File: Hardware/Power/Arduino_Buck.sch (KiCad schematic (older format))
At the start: 10 parts, among them Q3 2N7000, Q4 PJM2301PSA-S

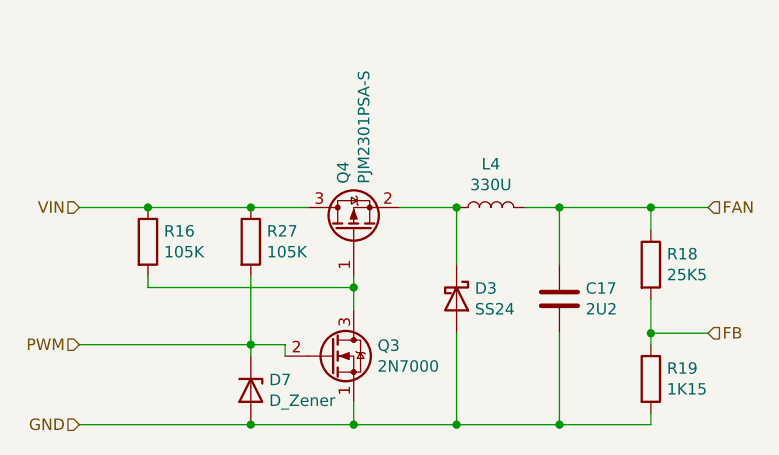
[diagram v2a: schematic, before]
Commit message: Fixed Power Board Errata
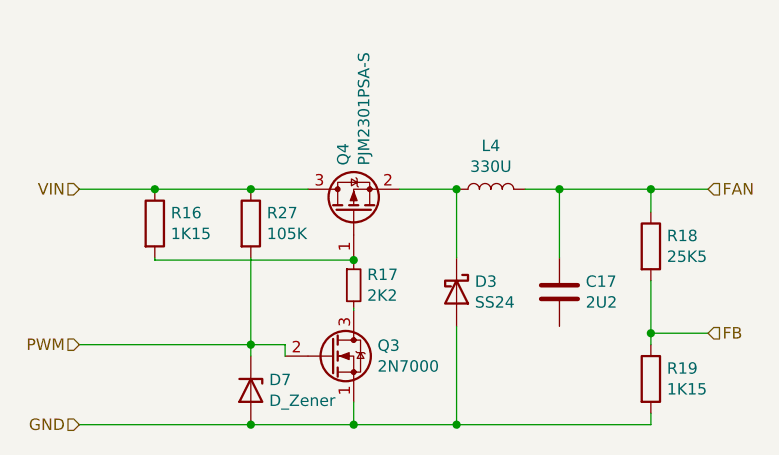
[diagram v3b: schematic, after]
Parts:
- added R17: 2K2, Resistor_SMD:R_0603_1608Metric_Pad1.05x0.95mm_HandSolder, symbol Device:R_Small
- R16: value 105K -> 1K15; Manufacturer_Part_Number RC0603FR-07105KL -> (none)
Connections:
- net GND: no longer C17.2
- net at Q4.1 (G), R16.2: now also R17.1; no longer Q3.3 (D)
- new net: Q3.3 (D), R17.2
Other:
- moved on the sheet: C17, D3, L4, Q4, R18, R27
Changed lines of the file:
@@
 $Descr A4 11693 8268
 encoding utf-8
-Sheet 5 7
+Sheet 4 7
 Title ""
 Date ""
@@
 Comment4 ""
 $EndDescr
-Text HLabel 4450 3450 0    50   Input ~ 0
-VIN
-Text HLabel 7200 3450 2    50   Input ~ 0
-FAN
 Text HLabel 4450 4400 0    50   Input ~ 0
 GND
 Text HLabel 7200 4000 2    50   Input ~ 0
 FB
-$Comp
-L Device:L L4
-U 1 1 5F8E9295
-P 6250 3450
-F 0 "L4" V 6440 3450 50  0000 C CNN
-F 1 "330U" V 6349 3450 50  0000 C CNN
-F 2 "ArduinoLamp:SLD10" H 6250 3450 50  0001 C CNN
-F 3 "~" H 6250 3450 50  0001 C CNN
-F 4 "SLD10D40S331MTT" H 6250 3450 50  0001 C CNN "Manufacturer_Part_Number"
-	1    6250 3450
-	0    -1   -1   0
-$EndComp
-$Comp
-L Device:D_Schottky D3
-U 1 1 5F8E9922
-P 6100 3850
-F 0 "D3" V 6054 3930 50  0000 L CNN
-F 1 "SS24" V 6145 3930 50  0000 L CNN
-F 2 "ArduinoLamp:D_SMA_Handsoldering_Shortened" H 6100 3850 50  0001 C CNN
-F 3 "~" H 6100 3850 50  0001 C CNN
-F 4 "" H 6100 3850 50  0001 C CNN "Mouser Part Number"
-F 5 "C181203" H 6100 3850 50  0001 C CNN "Arrow Part Number"
-	1    6100 3850
-	0    1    1    0
-$EndComp
-$Comp
-L Device:C C17
-U 1 1 5F8EC349
-P 6550 3850
-F 0 "C17" H 6665 3896 50  0000 L CNN
-F 1 "2U2" H 6665 3805 50  0000 L CNN
-F 2 "Capacitor_SMD:C_0805_2012Metric_Pad1.15x1.40mm_HandSolder" H 6588 3700 50  0001 C CNN
-F 3 "~" H 6550 3850 50  0001 C CNN
-F 4 "C0805X5R225K500NT" H 6550 3850 50  0001 C CNN "Manufacturer_Part_Number"
-	1    6550 3850
-	1    0    0    -1
-$EndComp
-$Comp
-L Device:R R18
-U 1 1 5F8ECD7F
-P 6950 3700
-F 0 "R18" H 7020 3746 50  0000 L CNN
-F 1 "25K5" H 7020 3655 50  0000 L CNN
-F 2 "Resistor_SMD:R_0603_1608Metric_Pad1.05x0.95mm_HandSolder" V 6880 3700 50  0001 C CNN
-F 3 "~" H 6950 3700 50  0001 C CNN
-F 4 "RS-05K2552FT" H 6950 3700 50  0001 C CNN "Manufacturer_Part_Number"
-	1    6950 3700
-	1    0    0    -1
-$EndComp
 $Comp
 L Device:R R19
@@
 Wire Wire Line
 	6950 4350 6950 4400
-Wire Wire Line
-	6950 4400 6550 4400
-Connection ~ 6550 4400
-Wire Wire Line
-	6550 3700 6550 3450
-Wire Wire Line
-	6550 3450 6950 3450
-Wire Wire Line
-	6950 3450 6950 3550
-Connection ~ 6950 3450
-Wire Wire Line
-	6950 3450 7200 3450
-Wire Wire Line
-	6400 3450 6550 3450
-Connection ~ 6550 3450
-Wire Wire Line
-	6100 3450 6100 3700
-$Comp
-L Device:R R27
-U 1 1 5FAF10C0
-P 5200 3600
-F 0 "R27" H 5270 3646 50  0000 L CNN
-F 1 "105K" H 5270 3555 50  0000 L CNN
-F 2 "Resistor_SMD:R_0603_1608Metric_Pad1.05x0.95mm_HandSolder" V 5130 3600 50  0001 C CNN
-F 3 "~" H 5200 3600 50  0001 C CNN
-F 4 "RC0603FR-07105KL" H 5200 3600 50  0001 C CNN "Manufacturer_Part_Number"
-	1    5200 3600
-	1    0    0    -1
-$EndComp
-$Comp
-L Device:R R16
-U 1 1 5F8FA0B3
-P 4750 3600
-F 0 "R16" H 4820 3646 50  0000 L CNN
-F 1 "105K" H 4820 3555 50  0000 L CNN
-F 2 "Resistor_SMD:R_0603_1608Metric_Pad1.05x0.95mm_HandSolder" V 4680 3600 50  0001 C CNN
-F 3 "~" H 4750 3600 50  0001 C CNN
-F 4 "RC0603FR-07105KL" H 4750 3600 50  0001 C CNN "Manufacturer_Part_Number"
-	1    4750 3600
-	1    0    0    -1
-$EndComp
 Connection ~ 5650 4400
-Connection ~ 6100 3450
-Wire Wire Line
-	5850 3450 6100 3450
 Connection ~ 6100 4400
-Wire Wire Line
-	6100 4400 6550 4400
 Wire Wire Line
 	5650 4400 6100 4400
@@
 	1    0    0    -1
 $EndComp
-Connection ~ 5200 3450
-Wire Wire Line
-	4450 3450 4750 3450
-Connection ~ 4750 3450
-Wire Wire Line
-	4750 3450 5200 3450
-Wire Wire Line
-	4750 3750 4750 3800
-Wire Wire Line
-	5200 3450 5450 3450
 Wire Wire Line
 	4450 4050 5200 4050
@@
 Wire Wire Line
 	5350 4050 5350 4100
-$Comp
-L Transistor_FET:TSM2301ACX Q4
-U 1 1 5F8E71B4
-P 5650 3550
-F 0 "Q4" H 5854 3596 50  0000 L CNN
-F 1 "PJM2301PSA-S" H 5854 3505 50  0000 L CNN
-F 2 "Package_TO_SOT_SMD:SOT-23" H 5850 3475 50  0001 L CIN
-F 3 "https://www.taiwansemi.com/products/datasheet/TSM2301A_C15.pdf" H 5650 3550 50  0001 L CNN
-F 4 "PJM2301PSA-S" H 5650 3550 50  0001 C CNN "Manufacturer_Part_Number"
-	1    5650 3550
-	0    -1   -1   0
-$EndComp
-Wire Wire Line
-	5200 3750 5200 4050
-Wire Wire Line
-	6100 4000 6100 4400
-Wire Wire Line
-	6550 4000 6550 4400
-Wire Wire Line
-	5650 3800 5650 3750
-Wire Wire Line
-	4750 3800 5650 3800
-Wire Wire Line
-	5650 3900 5650 3800
-Connection ~ 5650 3800
-Wire Wire Line
-	6950 3850 6950 4000
-Connection ~ 6950 4000
 Wire Wire Line
 	4450 4400 5200 4400
@@
 Wire Wire Line
 	5200 4400 5650 4400
+Wire Wire Line
+	4450 3370 4780 3370
+$Comp
+L Transistor_FET:TSM2301ACX Q4
+U 1 1 5F8E71B4
+P 5650 3470
+F 0 "Q4" H 5854 3516 50  0000 L CNN
+F 1 "PJM2301PSA-S" H 5854 3425 50  0000 L CNN
+F 2 "Package_TO_SOT_SMD:SOT-23" H 5850 3395 50  0001 L CIN
+F 3 "https://www.taiwansemi.com/products/datasheet/TSM2301A_C15.pdf" H 5650 3470 50  0001 L CNN
+F 4 "PJM2301PSA-S" H 5650 3470 50  0001 C CNN "Manufacturer_Part_Number"
+	1    5650 3470
+	0    -1   -1   0
+$EndComp
+Wire Wire Line
+	5200 3370 5450 3370
+Connection ~ 5200 3370
+Wire Wire Line
+	5850 3370 6100 3370
+$Comp
+L Device:R R27
+U 1 1 5FAF10C0
+P 5200 3520
+F 0 "R27" H 5270 3566 50  0000 L CNN
+F 1 "105K" H 5270 3475 50  0000 L CNN
+F 2 "Resistor_SMD:R_0603_1608Metric_Pad1.05x0.95mm_HandSolder" V 5130 3520 50  0001 C CNN
+F 3 "~" H 5200 3520 50  0001 C CNN
+F 4 "RC0603FR-07105KL" H 5200 3520 50  0001 C CNN "Manufacturer_Part_Number"
+	1    5200 3520
+	1    0    0    -1
+$EndComp
+Wire Wire Line
+	6950 3370 7200 3370
+Connection ~ 6950 3370
+Wire Wire Line
+	6950 3370 6950 3470
+$Comp
+L Device:R R18
+U 1 1 5F8ECD7F
+P 6950 3620
+F 0 "R18" H 7020 3666 50  0000 L CNN
+F 1 "25K5" H 7020 3575 50  0000 L CNN
+F 2 "Resistor_SMD:R_0603_1608Metric_Pad1.05x0.95mm_HandSolder" V 6880 3620 50  0001 C CNN
+F 3 "~" H 6950 3620 50  0001 C CNN
+F 4 "RS-05K2552FT" H 6950 3620 50  0001 C CNN "Manufacturer_Part_Number"
+	1    6950 3620
+	1    0    0    -1
+$EndComp
+$Comp
+L Device:C C17
+U 1 1 5F8EC349
+P 6550 3820
+F 0 "C17" H 6665 3866 50  0000 L CNN
+F 1 "2U2" H 6665 3775 50  0000 L CNN
+F 2 "Capacitor_SMD:C_0805_2012Metric_Pad1.15x1.40mm_HandSolder" H 6588 3670 50  0001 C CNN
+F 3 "~" H 6550 3820 50  0001 C CNN
+F 4 "C0805X5R225K500NT" H 6550 3820 50  0001 C CNN "Manufacturer_Part_Number"
+	1    6550 3820
+	1    0    0    -1
+$EndComp
+$Comp
+L Device:D_Schottky D3
+U 1 1 5F8E9922
+P 6100 3820
+F 0 "D3" V 6054 3900 50  0000 L CNN
+F 1 "SS24" V 6145 3900 50  0000 L CNN
+F 2 "ArduinoLamp:D_SMA_Handsoldering_Shortened" H 6100 3820 50  0001 C CNN
+F 3 "~" H 6100 3820 50  0001 C CNN
+F 4 "" H 6100 3820 50  0001 C CNN "Mouser Part Number"
+F 5 "C181203" H 6100 3820 50  0001 C CNN "Arrow Part Number"
+	1    6100 3820
+	0    1    1    0
+$EndComp
+$Comp
+L Device:L L4
+U 1 1 5F8E9295
+P 6250 3370
+F 0 "L4" V 6440 3370 50  0000 C CNN
+F 1 "330U" V 6349 3370 50  0000 C CNN
+F 2 "ArduinoLamp:SLD10" H 6250 3370 50  0001 C CNN
+F 3 "~" H 6250 3370 50  0001 C CNN
+F 4 "SLD10D40S331MTT" H 6250 3370 50  0001 C CNN "Manufacturer_Part_Number"
+	1    6250 3370
+	0    -1   -1   0
+$EndComp
+Text HLabel 7200 3370 2    50   Input ~ 0
+FAN
+Text HLabel 4450 3370 0    50   Input ~ 0
+VIN
+$Comp
+L Device:R_Small R17
+U 1 1 5FCEBA9D
+P 5650 3790
+F 0 "R17" H 5709 3836 50  0000 L CNN
+F 1 "2K2" H 5709 3745 50  0000 L CNN
+F 2 "Resistor_SMD:R_0603_1608Metric_Pad1.05x0.95mm_HandSolder" H 5650 3790 50  0001 C CNN
+F 3 "~" H 5650 3790 50  0001 C CNN
+	1    5650 3790
+	1    0    0    -1
+$EndComp
+Wire Wire Line
+	6950 3770 6950 4000
+Connection ~ 6950 4000
+Wire Wire Line
+	5200 3670 5200 4050
+Wire Wire Line
+	5650 3890 5650 3900
+Wire Wire Line
+	5650 3690 5650 3680
+$Comp
+L Device:R R16
+U 1 1 5FCF08E2
+P 4780 3520
+F 0 "R16" H 4850 3566 50  0000 L CNN
+F 1 "1K15" H 4850 3475 50  0000 L CNN
+F 2 "Resistor_SMD:R_0603_1608Metric_Pad1.05x0.95mm_HandSolder" V 4710 3520 50  0001 C CNN
+F 3 "~" H 4780 3520 50  0001 C CNN
+	1    4780 3520
+	1    0    0    -1
+$EndComp
+Connection ~ 4780 3370
+Wire Wire Line
+	4780 3370 5200 3370
+Wire Wire Line
+	4780 3670 4780 3680
+Wire Wire Line
+	4780 3680 5650 3680
+Connection ~ 5650 3680
+Wire Wire Line
+	5650 3680 5650 3670
+Wire Wire Line
+	6400 3370 6550 3370
+Wire Wire Line
+	6100 4400 6950 4400
+Wire Wire Line
+	6100 3970 6100 4400
+Wire Wire Line
+	6100 3670 6100 3370
+Connection ~ 6100 3370
+Wire Wire Line
+	6550 3670 6550 3370
+Connection ~ 6550 3370
+Wire Wire Line
+	6550 3370 6950 3370
 $EndSCHEMATC
